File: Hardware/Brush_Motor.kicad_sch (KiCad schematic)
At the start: 66 parts, among them IC1 EA3036QBR, IC10 HY2213-BB3A, IC11 HY2213-BB3A, IC12 HY2213-BB3A, IC13 HY2213-BB3A, IC2 TPS5450DDAR, Q2 AO3401A, Q3 AO3400, Q4 AO3400, Q5 AO3400, Q6 AO3400

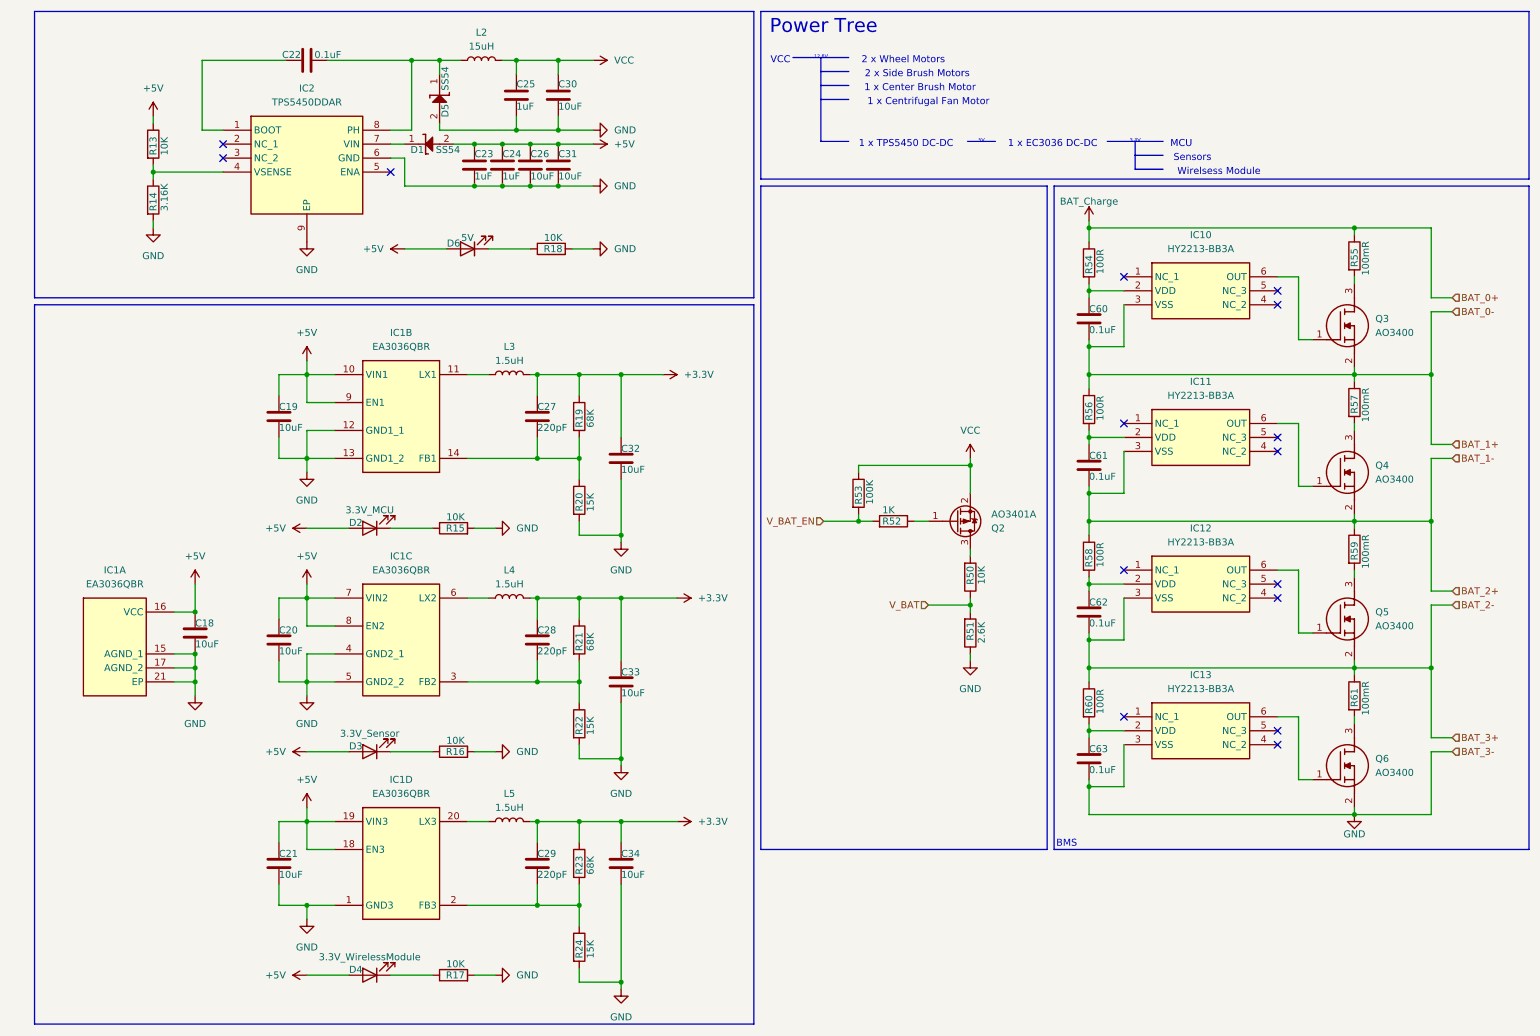
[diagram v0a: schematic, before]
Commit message: Add Image Transmission
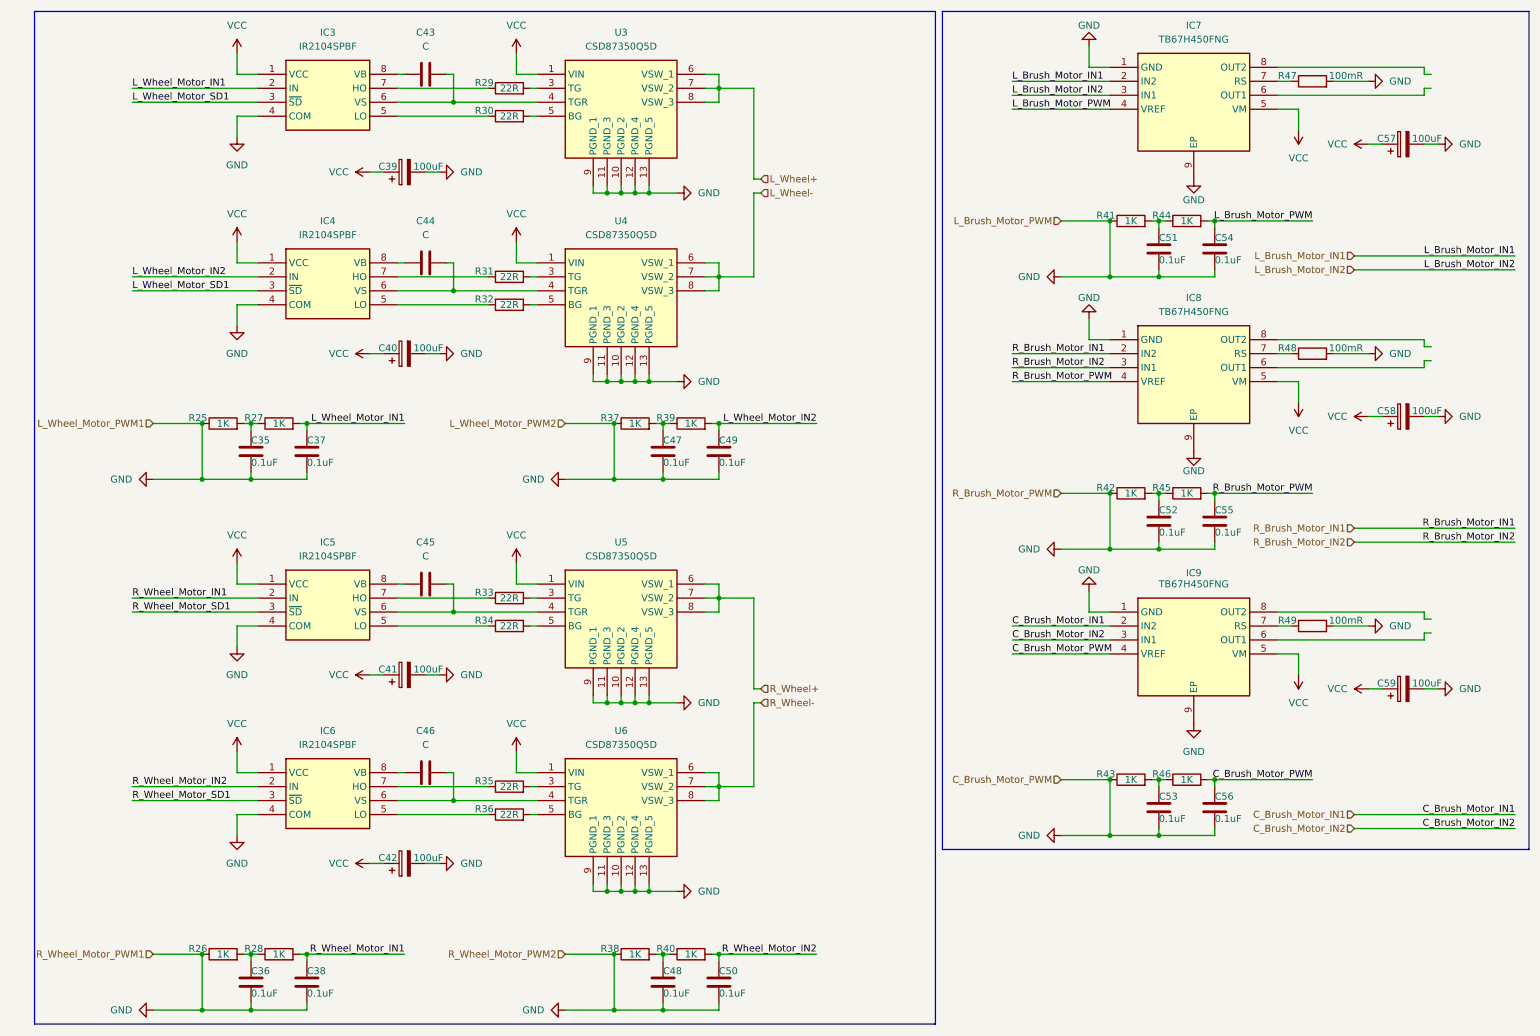
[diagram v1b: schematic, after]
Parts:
- removed C18, C19, C20, C21, C26, C30, C31, C32, C33, C34: 10uF, symbol Device:C
- removed C22, C60, C61, C62, C63: 0.1uF, symbol Device:C
- removed C23, C24, C25: 1uF, symbol Device:C
- removed C27, C28, C29: 220pF, symbol Device:C
- removed D1, D5: SS54, DIOM5126X245N, symbol SamacSys_Parts:SS54
- removed D2: 3.3V_MCU, symbol Device:LED
- removed D3: 3.3V_Sensor, symbol Device:LED
- removed D4: 3.3V_WirelessModule, symbol Device:LED
- removed D6: 5V, symbol Device:LED
- removed IC1: EA3036QBR, QFN40P300X300X80-21N, symbol SamacSys_Parts:EA3036QBR
- removed IC10, IC11, IC12, IC13: HY2213-BB3A, SOT95P280X140-6N, symbol SamacSys_Parts:HY2213-BB3A
- removed IC2: TPS5450DDAR, SOIC127P600X170-9N, symbol SamacSys_Parts:TPS5450DDAR
- removed L2: 15uH, symbol Device:L
- removed L3, L4, L5: 1.5uH, symbol Device:L
- removed Q2: AO3401A, Package_TO_SOT_SMD:SOT-23, symbol Transistor_FET:AO3401A
- removed Q3, Q4, Q5, Q6: AO3400, SOT95P280X125-3N, symbol SamacSys_Parts:AO3400
- removed R13, R15, R16, R17, R18, R50: 10K, symbol Device:R
- removed R14: 3.16K, symbol Device:R
- removed R19, R21, R23: 68K, symbol Device:R
- removed R20, R22, R24: 15K, symbol Device:R
- removed R51: 2.6K, symbol Device:R
- removed R52: 1K, symbol Device:R
- removed R53: 100K, symbol Device:R
- removed R54, R56, R58, R60: 100R, symbol Device:R
- removed R55, R57, R59, R61: 100mR, symbol Device:R
- added C35, C36, C37, C38, C47, C48, C49, C50, C51, C52, C53, C54, C55, C56: 0.1uF, symbol Device:C
- added C39, C40, C41, C42, C57, C58, C59: 100uF, Capacitor_SMD:CP_Elec_6.3x7.7, symbol Device:C_Polarized
- added C43, C44, C45, C46: C, symbol Device:C
- added IC3, IC4, IC5, IC6: IR2104SPBF, SOIC127P600X175-8N, symbol SamacSys_Parts:IR2104SPBF
- added IC7, IC8, IC9: TB67H450FNG, SOIC127P600X175-9N, symbol SamacSys_Parts:TB67H450FNG
- added R25, R26, R27, R28, R37, R38, R39, R40, R41, R42, R43, R44, R45, R46: 1K, symbol Device:R
- added R29, R30, R31, R32, R33, R34, R35, R36: 22R, symbol Device:R
- added R47, R48, R49: 100mR, symbol Device:R
- added U3, U4, U5, U6: CSD87350Q5D, CSD87350Q5D, symbol SamacSys_Parts:CSD87350Q5D
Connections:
- net GND: now also C35.1, C36.1, C37.1, C38.1, C39.2, C40.2, C41.2, C42.2, C47.1, C48.1, C49.1, C50.1, C51.1, C52.1, C53.1, C54.1, C54.2, C55.1, C55.2, C56.1, C56.2, C57.2, C58.2, C59.2, IC3.4 (COM), IC4.4 (COM), IC5.4 (COM), IC6.4 (COM), IC7.1 (GND), IC7.4 (VREF), IC7.9 (EP), IC8.1 (GND), IC8.4 (VREF), IC8.9 (EP), IC9.1 (GND), IC9.4 (VREF), IC9.9 (EP), R25.1, R26.1, R37.1, R38.1, R41.1, R42.1, R43.1, R44.2, R45.2, R46.2, R47.2, R48.2, R49.2, U3.10 (PGND_2), U3.11 (PGND_3), U3.12 (PGND_4), U3.13 (PGND_5), U3.9 (PGND_1), U4.10 (PGND_2), U4.11 (PGND_3), U4.12 (PGND_4), U4.13 (PGND_5), U4.9 (PGND_1), U5.10 (PGND_2), U5.11 (PGND_3), U5.12 (PGND_4), U5.13 (PGND_5), U5.9 (PGND_1), U6.10 (PGND_2), U6.11 (PGND_3), U6.12 (PGND_4), U6.13 (PGND_5), U6.9 (PGND_1)
- net VCC: now also C39.1, C40.1, C41.1, C42.1, C57.1, C58.1, C59.1, IC3.1 (VCC), IC4.1 (VCC), IC5.1 (VCC), IC6.1 (VCC), IC7.5 (VM), IC8.5 (VM), IC9.5 (VM), U3.1 (VIN), U4.1 (VIN), U5.1 (VIN), U6.1 (VIN)
- new net: IC7.7 (RS), R47.1
- new net: C52.2, R42.2, R45.1
- new net: IC9.7 (RS), R49.1
- new net: C36.2, R26.2, R28.1
- new net: C51.2, R41.2, R44.1
- new net: R35.2, U6.3 (TG)
- new net: C46.2, IC6.6 (VS), U6.4 (TGR)
- new net: R36.2, U6.5 (BG)
- new net: C35.2, R25.2, R27.1
- new net: IC5.5 (LO), R34.1
- new net: C45.2, IC5.6 (VS), U5.4 (TGR)
- new net: IC5.7 (HO), R33.1
- new net: C45.1, IC5.8 (VB)
- new net: C53.2, R43.2, R46.1
- new net: IC3.7 (HO), R29.1
- new net: R29.2, U3.3 (TG)
- new net: R31.2, U4.3 (TG)
- new net: C44.2, IC4.6 (VS), U4.4 (TGR)
- new net: R32.2, U4.5 (BG)
- new net: C48.2, R38.2, R40.1
- new net: C47.2, R37.2, R39.1
- new net: IC3.5 (LO), R30.1
- new net: C43.2, IC3.6 (VS), U3.4 (TGR)
- new net: C43.1, IC3.8 (VB)
- new net: IC6.5 (LO), R36.1
- new net: IC6.7 (HO), R35.1
- new net: C46.1, IC6.8 (VB)
- new net: C44.1, IC4.8 (VB)
- new net: R33.2, U5.3 (TG)
- new net: R34.2, U5.5 (BG)
- new net: IC4.7 (HO), R31.1
- new net: R30.2, U3.5 (BG)
- new net: IC4.5 (LO), R32.1
- new net: IC8.7 (RS), R48.1
- new net C_Brush_Motor_IN1: IC9.2 (IN2)
- new net C_Brush_Motor_IN2: IC9.3 (IN1)
- new net L_Brush_Motor_IN1: IC7.2 (IN2)
- new net L_Brush_Motor_IN2: IC7.3 (IN1)
- new net L_Wheel+: U3.6 (VSW_1), U3.7 (VSW_2), U3.8 (VSW_3)
- new net L_Wheel-: U4.6 (VSW_1), U4.7 (VSW_2), U4.8 (VSW_3)
- new net L_Wheel_Motor_IN1: C37.2, IC3.2 (IN), R27.2
- new net L_Wheel_Motor_IN2: C49.2, IC4.2 (IN), R39.2
- new net L_Wheel_Motor_SD1: IC3.3 (~{SD}), IC4.3 (~{SD})
- new net R_Brush_Motor_IN1: IC8.2 (IN2)
- new net R_Brush_Motor_IN2: IC8.3 (IN1)
- new net R_Wheel+: U5.6 (VSW_1), U5.7 (VSW_2), U5.8 (VSW_3)
- new net R_Wheel-: U6.6 (VSW_1), U6.7 (VSW_2), U6.8 (VSW_3)
- new net R_Wheel_Motor_IN1: C38.2, IC5.2 (IN), R28.2
- new net R_Wheel_Motor_IN2: C50.2, IC6.2 (IN), R40.2
- new net R_Wheel_Motor_SD1: IC5.3 (~{SD}), IC6.3 (~{SD})
- no-connect marks 15 -> 0
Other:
- note removed: "1 x Center Brush Motor"
- note removed: "1 x Centrifugal Fan Motor"
- note removed: "1 x EC3036 DC-DC"
- note removed: "1 x TPS5450 DC-DC"
- note removed: "12.6V"
- note removed: "2 x Side Brush Motors"
- note removed: "2 x Wheel Motors"
- note removed: "3.3V"
- note removed: "5V"
- note removed: "BMS"
- note removed: "MCU"
- note removed: "Power Tree"
- note removed: "Sensors"
- note removed: "VCC"
- note removed: "Wirelsess Module"
- title: Power_Manager -> (none)

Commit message: Update SCH
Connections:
- net L_Brush-: now reaches IC7.6 (OUT1)
- net L_Brush+: now reaches IC7.8 (OUT2)
- net C_Brush-: now reaches IC9.6 (OUT1)
- net C_Brush+: now reaches IC9.8 (OUT2)
- net R_Brush-: now reaches IC8.6 (OUT1)
- net R_Brush+: now reaches IC8.8 (OUT2)
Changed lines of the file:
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@@
 		)
 	)
+	(hierarchical_label "C_Brush+"
+		(shape input)
+		(at 266.7 123.19 0)
+		(fields_autoplaced yes)
+		(effects
+			(font
+				(size 1.27 1.27)
+			)
+			(justify left)
+		)
+	)
 	(hierarchical_label "C_Brush_Motor_IN2"
 		(shape input)
@@
 		)
 	)
+	(hierarchical_label "L_Brush+"
+		(shape input)
+		(at 266.7 24.13 0)
+		(fields_autoplaced yes)
+		(effects
+			(font
+				(size 1.27 1.27)
+			)
+			(justify left)
+		)
+	)
 	(hierarchical_label "R_Brush_Motor_IN2"
 		(shape input)
@@
 		)
 	)
+	(hierarchical_label "C_Brush-"
+		(shape input)
+		(at 266.7 125.73 0)
+		(fields_autoplaced yes)
+		(effects
+			(font
+				(size 1.27 1.27)
+			)
+			(justify left)
+		)
+	)
 	(hierarchical_label "R_Wheel_Motor_PWM1"
 		(shape input)
@@
 		)
 	)
+	(hierarchical_label "L_Brush-"
+		(shape input)
+		(at 266.7 26.67 0)
+		(fields_autoplaced yes)
+		(effects
+			(font
+				(size 1.27 1.27)
+			)
+			(justify left)
+		)
+	)
 	(hierarchical_label "R_Wheel-"
 		(shape input)
@@
 		)
 	)
+	(hierarchical_label "R_Brush-"
+		(shape input)
+		(at 266.7 76.2 0)
+		(fields_autoplaced yes)
+		(effects
+			(font
+				(size 1.27 1.27)
+			)
+			(justify left)
+		)
+	)
 	(hierarchical_label "L_Wheel+"
 		(shape input)
@@
 		)
 	)
+	(hierarchical_label "R_Brush+"
+		(shape input)
+		(at 266.7 73.66 0)
+		(fields_autoplaced yes)
+		(effects
+			(font
+				(size 1.27 1.27)
+			)
+			(justify left)
+		)
+	)
 	(hierarchical_label "R_Wheel_Motor_PWM2"
 		(shape input)
@@
 		)
 		(instances
-			(project ""
+			(project "Hardware"
 				(path "/8d39550c-1c23-48e1-ae23-c502e9088467/40bedbed-9ca5-4597-b8a7-97da2cb44045"
 					(reference "IC7")
@@
 		)
 		(instances
-			(project ""
+			(project "Hardware"
 				(path "/8d39550c-1c23-48e1-ae23-c502e9088467/40bedbed-9ca5-4597-b8a7-97da2cb44045"
 					(reference "C39")
@@
 		)
 		(instances
-			(project ""
+			(project "Hardware"
 				(path "/8d39550c-1c23-48e1-ae23-c502e9088467/40bedbed-9ca5-4597-b8a7-97da2cb44045"
 					(reference "R29")
@@
 		)
 		(instances
-			(project ""
+			(project "Hardware"
 				(path "/8d39550c-1c23-48e1-ae23-c502e9088467/40bedbed-9ca5-4597-b8a7-97da2cb44045"
 					(reference "C43")
@@
 		)
 		(instances
-			(project ""
+			(project "Hardware"
 				(path "/8d39550c-1c23-48e1-ae23-c502e9088467/40bedbed-9ca5-4597-b8a7-97da2cb44045"
 					(reference "#PWR062")
@@
 		)
 		(instances
-			(project ""
+			(project "Hardware"
 				(path "/8d39550c-1c23-48e1-ae23-c502e9088467/40bedbed-9ca5-4597-b8a7-97da2cb44045"
 					(reference "#PWR061")

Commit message: Update PCB
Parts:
- C35, C36, C37, C38, C47, C48, C49, C50, C51, C52, C53, C54, C55, C56: footprint (none) -> Capacitor_SMD:C_0603_1608Metric; symbol Device:C -> Library:C
- C39, C40, C41, C42, C57, C58, C59: footprint Capacitor_SMD:CP_Elec_6.3x7.7 -> SamacSys_Parts:CAPPM3528X210N; symbol Device:C_Polarized -> Library:C_Polarized
- C43, C44, C45, C46: value C -> 1uF; footprint (none) -> Capacitor_SMD:C_0603_1608Metric; symbol Device:C -> Library:C
- IC3, IC4, IC5, IC6: symbol SamacSys_Parts:IR2104SPBF -> Library:IR2104SPBF
- IC7, IC8, IC9: symbol SamacSys_Parts:TB67H450FNG -> Library:TB67H450FNG
- R25, R26, R27, R28, R29, R30, R31, R32, R33, R34, R35, R36, R37, R38, R39, R40, R41, R42, R43, R44, R45, R46: footprint (none) -> Resistor_SMD:R_0603_1608Metric; symbol Device:R -> Library:R
- R47, R48, R49: footprint (none) -> Resistor_SMD:R_1206_3216Metric; symbol Device:R -> Library:R
- U3, U4, U5, U6: symbol SamacSys_Parts:CSD87350Q5D -> Library:CSD87350Q5D
